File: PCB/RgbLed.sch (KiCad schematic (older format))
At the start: 7 parts, among them Q1 BC817, Q2 BC817, Q3 BC817

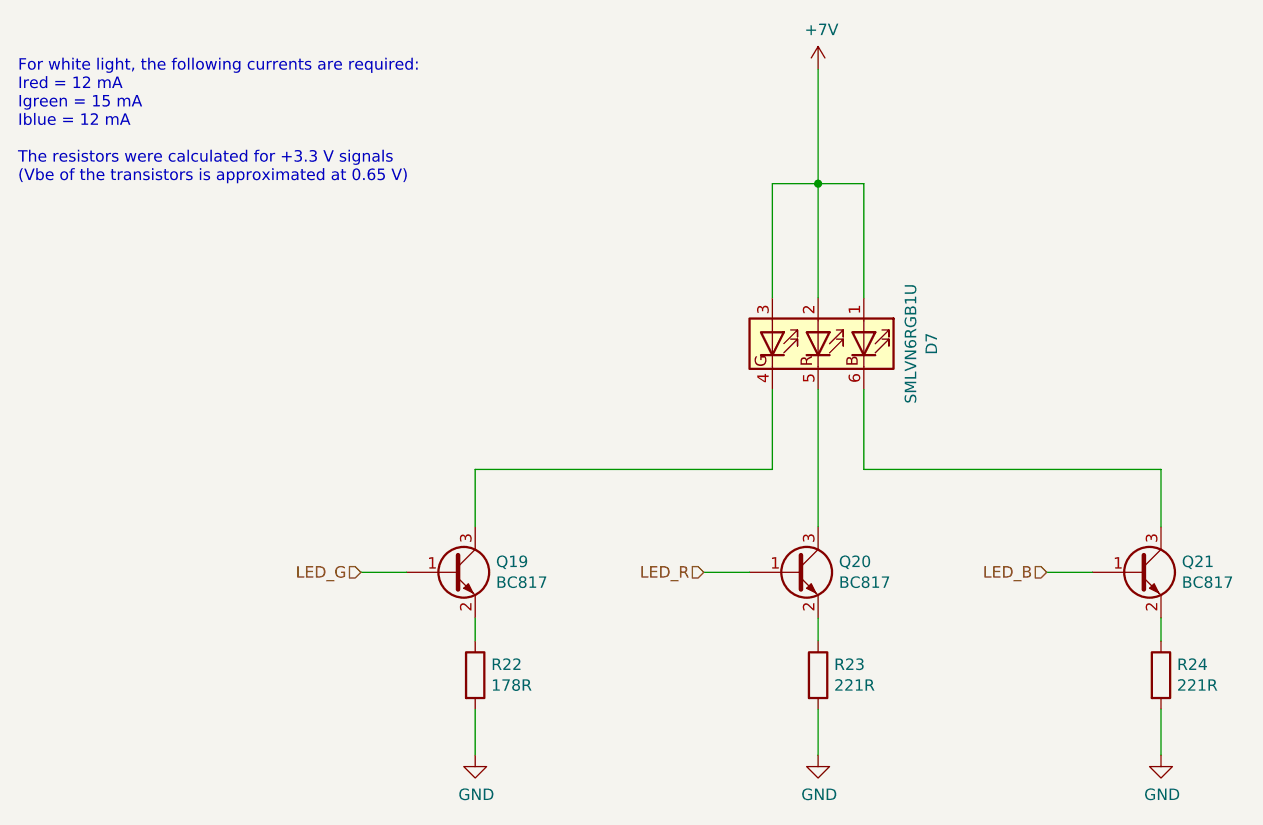
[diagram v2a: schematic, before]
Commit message: Improve the push buttons
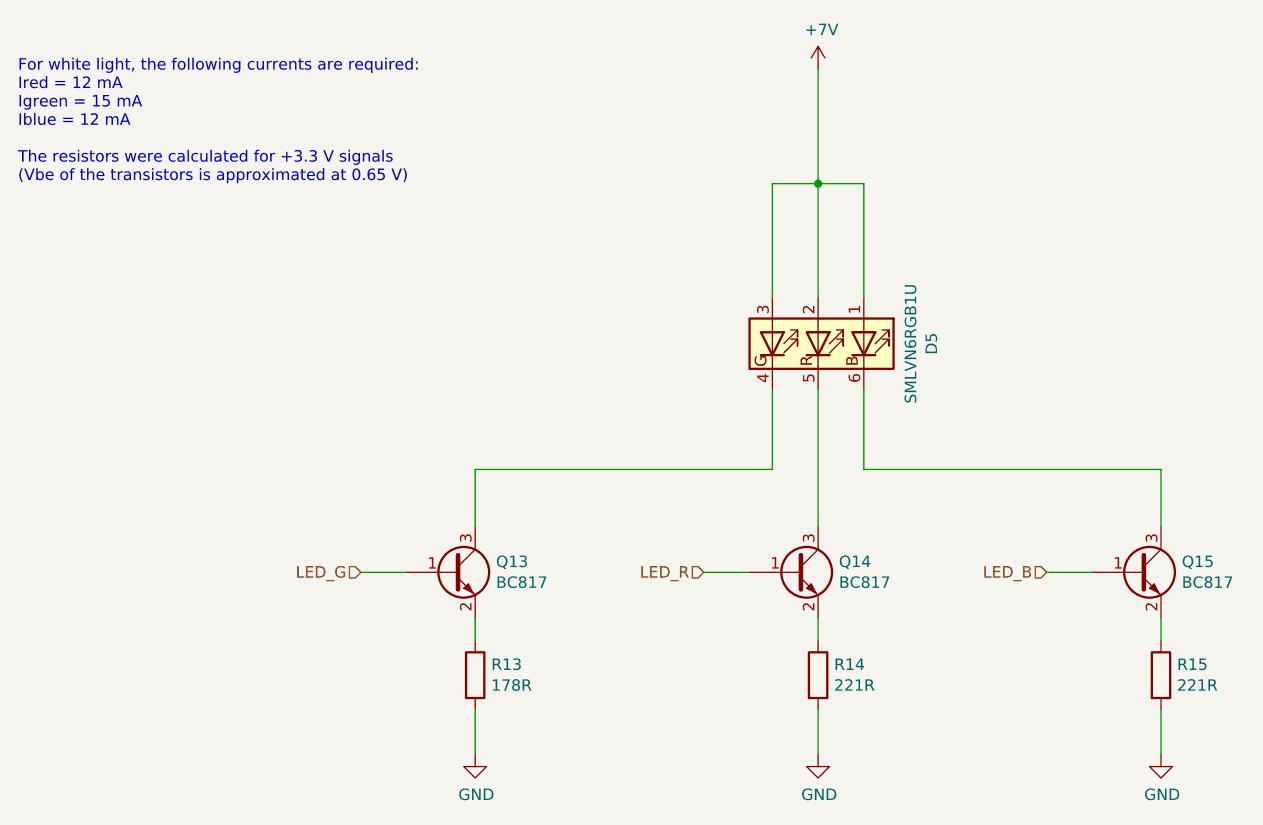
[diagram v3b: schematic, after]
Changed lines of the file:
@@
 $Descr A4 11693 8268
 encoding utf-8
-Sheet 12 19
+Sheet 7 19
 Title "Litter Robot 3 - RGB LED"
 Date "2021-03-28"
@@
 AR Path="/603F1F4D/605BE11A/603E2469" Ref="Q?"  Part="1"
 AR Path="/603F1F4D/605BE15A/603E2469" Ref="Q?"  Part="1"
-F 0 "Q19" H 4091 4246 50  0000 L CNN
+F 0 "Q13" H 4091 4246 50  0000 L CNN
 F 1 "BC817" H 4091 4155 50  0000 L CNN
 F 2 "Package_TO_SOT_SMD:SOT-23" H 4100 4125 50  0001 L CIN
@@
 AR Path="/603F1F4D/605BE11A/603E246F" Ref="R?"  Part="1"
 AR Path="/603F1F4D/605BE15A/603E246F" Ref="R?"  Part="1"
-F 0 "R22" H 4070 4696 50  0000 L CNN
+F 0 "R13" H 4070 4696 50  0000 L CNN
 F 1 "178R" H 4070 4605 50  0000 L CNN
 F 2 "Resistor_SMD:R_0603_1608Metric" V 3930 4650 50  0001 C CNN
@@
 AR Path="/603F1F4D/605BE11A/603E7162" Ref="D?"  Part="1"
 AR Path="/603F1F4D/605BE15A/603E7162" Ref="D?"  Part="1"
-F 0 "D7" H 5500 3697 50  0000 C CNN
+F 0 "D5" H 5500 3697 50  0000 C CNN
 F 1 "SMLVN6RGB1U" H 5500 3606 50  0000 C CNN
 F 2 "LitterRobot:ROHM_SMLVN6" H 5500 2850 50  0001 C CNN
@@
 AR Path="/603F1F4D/605BE11A/603FCE1E" Ref="R?"  Part="1"
 AR Path="/603F1F4D/605BE15A/603FCE1E" Ref="R?"  Part="1"
-F 0 "R23" H 5570 4696 50  0000 L CNN
+F 0 "R14" H 5570 4696 50  0000 L CNN
 F 1 "221R" H 5570 4605 50  0000 L CNN
 F 2 "Resistor_SMD:R_0603_1608Metric" V 5430 4650 50  0001 C CNN
@@
 AR Path="/603F1F4D/605BE11A/603FDBA6" Ref="R?"  Part="1"
 AR Path="/603F1F4D/605BE15A/603FDBA6" Ref="R?"  Part="1"
-F 0 "R24" H 7070 4696 50  0000 L CNN
+F 0 "R15" H 7070 4696 50  0000 L CNN
 F 1 "221R" H 7070 4605 50  0000 L CNN
 F 2 "Resistor_SMD:R_0603_1608Metric" V 6930 4650 50  0001 C CNN
@@
 AR Path="/603F1F4D/605BE11A/6045060B" Ref="Q?"  Part="1"
 AR Path="/603F1F4D/605BE15A/6045060B" Ref="Q?"  Part="1"
-F 0 "Q20" H 5591 4246 50  0000 L CNN
+F 0 "Q14" H 5591 4246 50  0000 L CNN
 F 1 "BC817" H 5591 4155 50  0000 L CNN
 F 2 "Package_TO_SOT_SMD:SOT-23" H 5600 4125 50  0001 L CIN
@@
 AR Path="/603F1F4D/605BE11A/60450E24" Ref="Q?"  Part="1"
 AR Path="/603F1F4D/605BE15A/60450E24" Ref="Q?"  Part="1"
-F 0 "Q21" H 7091 4246 50  0000 L CNN
+F 0 "Q15" H 7091 4246 50  0000 L CNN
 F 1 "BC817" H 7091 4155 50  0000 L CNN
 F 2 "Package_TO_SOT_SMD:SOT-23" H 7100 4125 50  0001 L CIN

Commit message: Add reverse polarity protection diodes
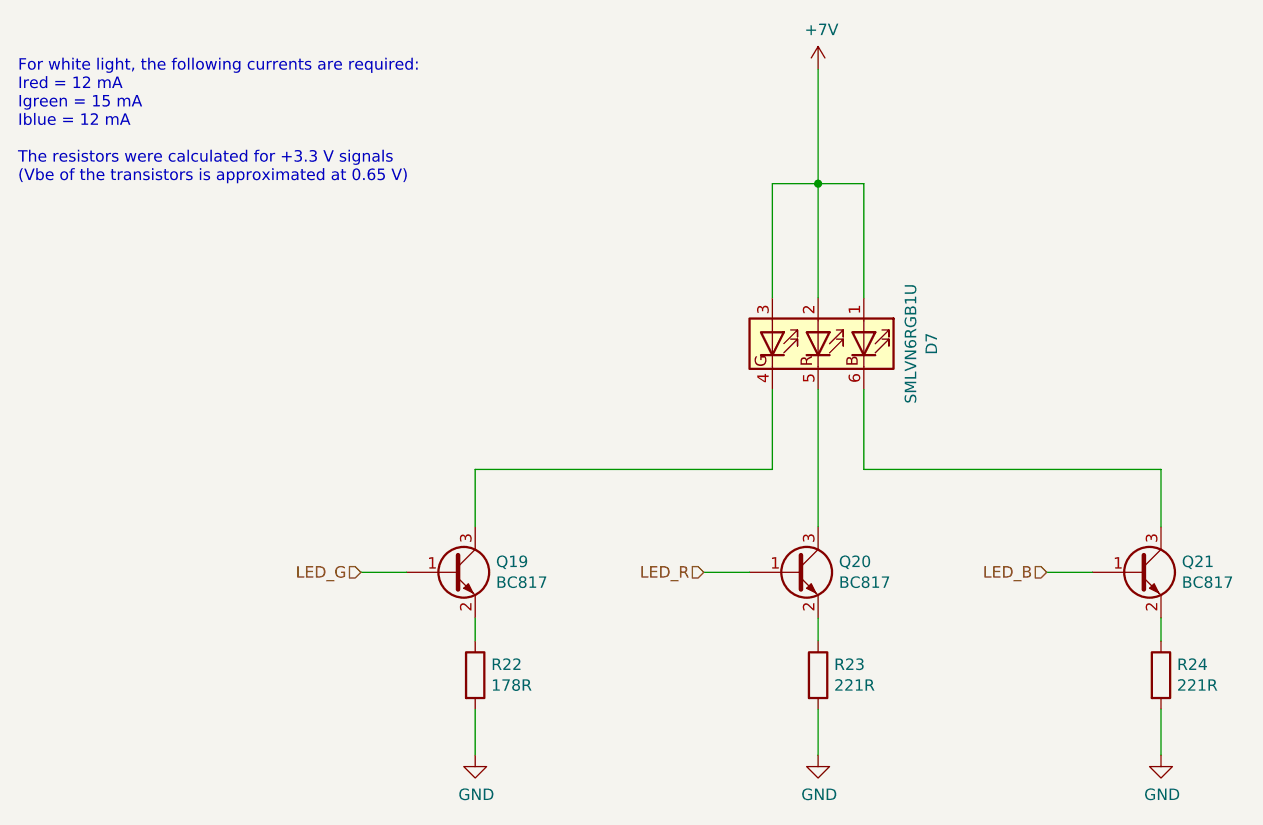
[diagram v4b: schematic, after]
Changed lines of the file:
@@
 AR Path="/603F1F4D/605BE11A/603E2469" Ref="Q?"  Part="1"
 AR Path="/603F1F4D/605BE15A/603E2469" Ref="Q?"  Part="1"
-F 0 "Q13" H 4091 4246 50  0000 L CNN
+F 0 "Q19" H 4091 4246 50  0000 L CNN
 F 1 "BC817" H 4091 4155 50  0000 L CNN
 F 2 "Package_TO_SOT_SMD:SOT-23" H 4100 4125 50  0001 L CIN
@@
 AR Path="/603F1F4D/605BE11A/603E246F" Ref="R?"  Part="1"
 AR Path="/603F1F4D/605BE15A/603E246F" Ref="R?"  Part="1"
-F 0 "R13" H 4070 4696 50  0000 L CNN
+F 0 "R22" H 4070 4696 50  0000 L CNN
 F 1 "178R" H 4070 4605 50  0000 L CNN
 F 2 "Resistor_SMD:R_0603_1608Metric" V 3930 4650 50  0001 C CNN
@@
 AR Path="/603F1F4D/605BE11A/603E7162" Ref="D?"  Part="1"
 AR Path="/603F1F4D/605BE15A/603E7162" Ref="D?"  Part="1"
-F 0 "D5" H 5500 3697 50  0000 C CNN
+F 0 "D7" H 5500 3697 50  0000 C CNN
 F 1 "SMLVN6RGB1U" H 5500 3606 50  0000 C CNN
 F 2 "LitterRobot:ROHM_SMLVN6" H 5500 2850 50  0001 C CNN
@@
 AR Path="/603F1F4D/605BE11A/603FCE1E" Ref="R?"  Part="1"
 AR Path="/603F1F4D/605BE15A/603FCE1E" Ref="R?"  Part="1"
-F 0 "R14" H 5570 4696 50  0000 L CNN
+F 0 "R23" H 5570 4696 50  0000 L CNN
 F 1 "221R" H 5570 4605 50  0000 L CNN
 F 2 "Resistor_SMD:R_0603_1608Metric" V 5430 4650 50  0001 C CNN
@@
 AR Path="/603F1F4D/605BE11A/603FDBA6" Ref="R?"  Part="1"
 AR Path="/603F1F4D/605BE15A/603FDBA6" Ref="R?"  Part="1"
-F 0 "R15" H 7070 4696 50  0000 L CNN
+F 0 "R24" H 7070 4696 50  0000 L CNN
 F 1 "221R" H 7070 4605 50  0000 L CNN
 F 2 "Resistor_SMD:R_0603_1608Metric" V 6930 4650 50  0001 C CNN
@@
 AR Path="/603F1F4D/605BE11A/6045060B" Ref="Q?"  Part="1"
 AR Path="/603F1F4D/605BE15A/6045060B" Ref="Q?"  Part="1"
-F 0 "Q14" H 5591 4246 50  0000 L CNN
+F 0 "Q20" H 5591 4246 50  0000 L CNN
 F 1 "BC817" H 5591 4155 50  0000 L CNN
 F 2 "Package_TO_SOT_SMD:SOT-23" H 5600 4125 50  0001 L CIN
@@
 AR Path="/603F1F4D/605BE11A/60450E24" Ref="Q?"  Part="1"
 AR Path="/603F1F4D/605BE15A/60450E24" Ref="Q?"  Part="1"
-F 0 "Q15" H 7091 4246 50  0000 L CNN
+F 0 "Q21" H 7091 4246 50  0000 L CNN
 F 1 "BC817" H 7091 4155 50  0000 L CNN
 F 2 "Package_TO_SOT_SMD:SOT-23" H 7100 4125 50  0001 L CIN

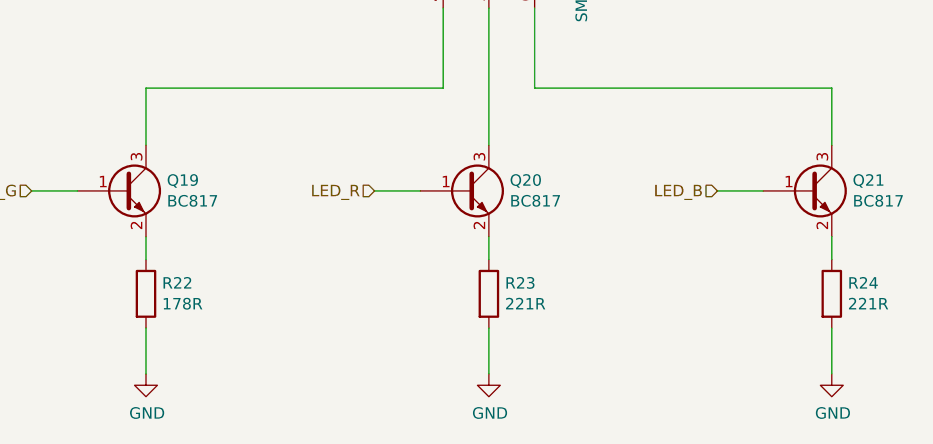
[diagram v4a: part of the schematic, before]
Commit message: Add support for the weight sensor
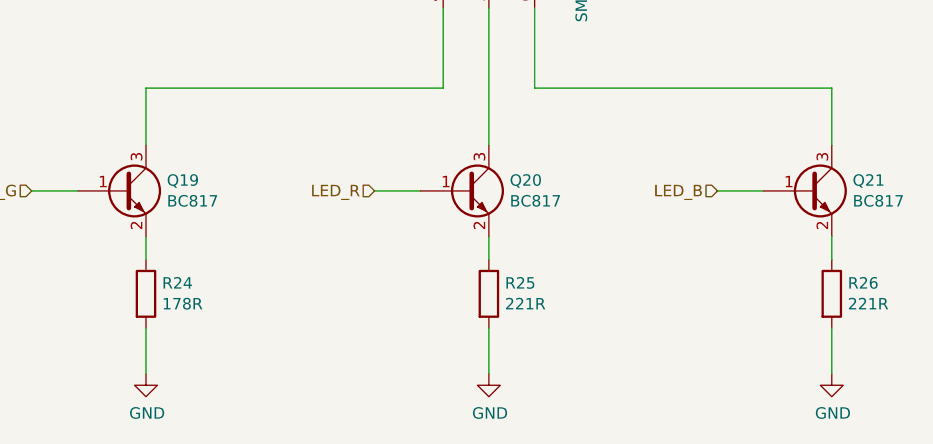
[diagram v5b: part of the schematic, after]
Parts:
- renumbered R1 to R3, R2 to R4, R3 to R5

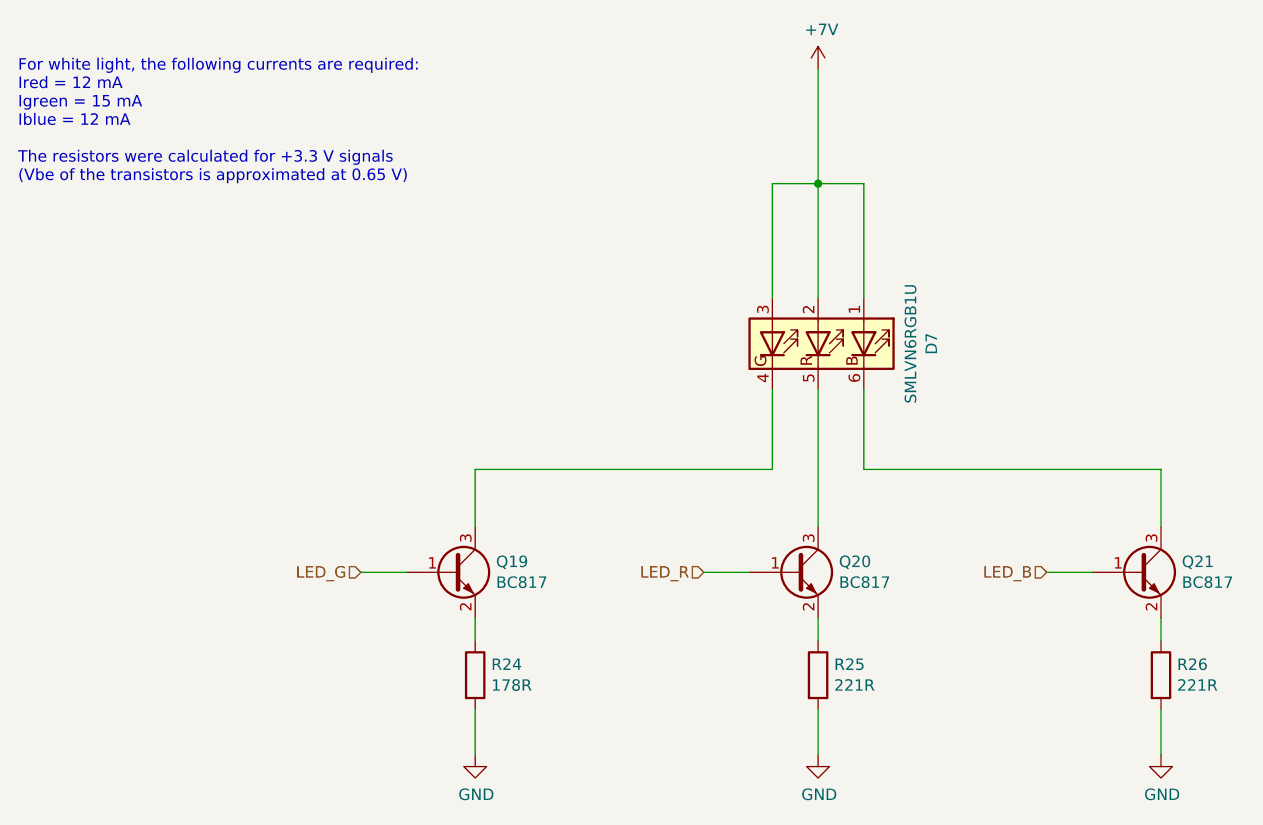
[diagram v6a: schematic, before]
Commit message: Re-annotate all components
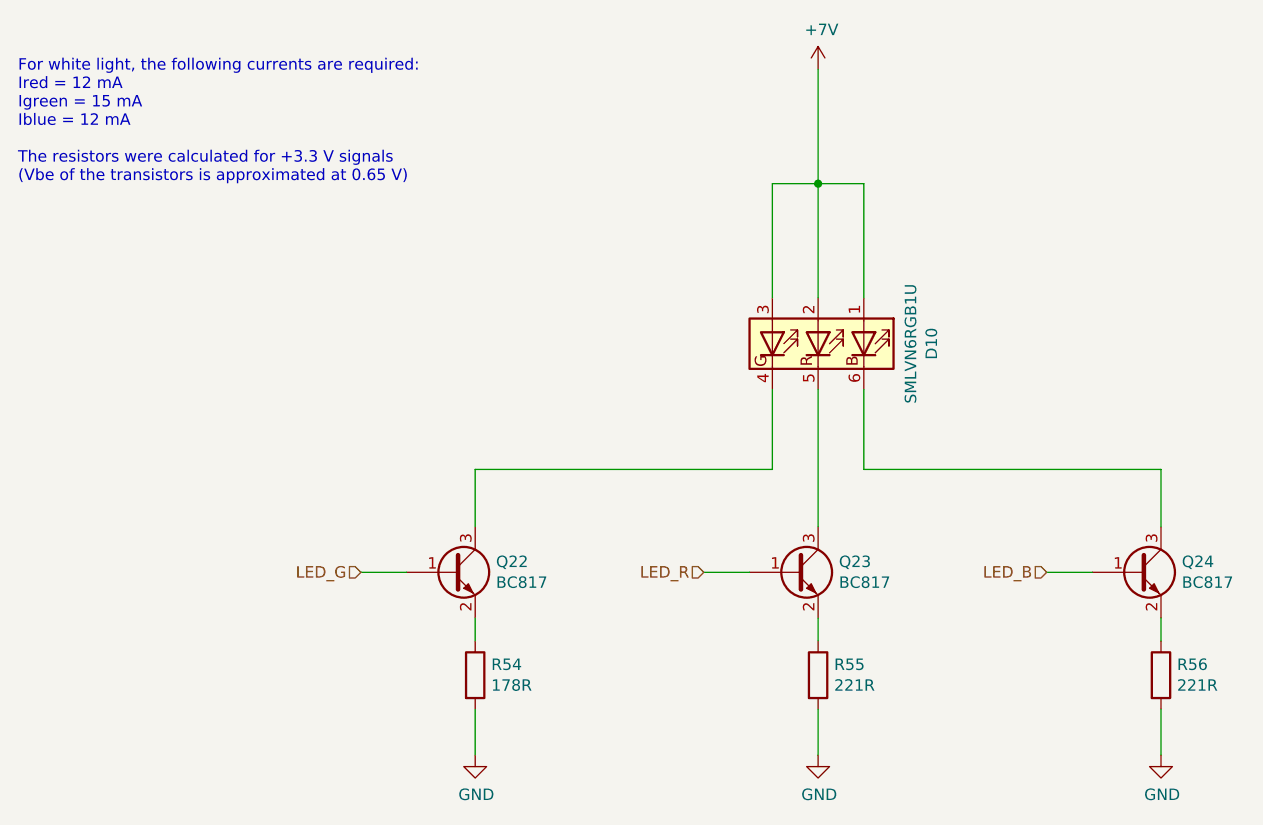
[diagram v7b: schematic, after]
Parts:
- renumbered D1 to D8, Q1 to Q16, Q2 to Q17, Q3 to Q18, R3 to R48, R4 to R49, R5 to R50
